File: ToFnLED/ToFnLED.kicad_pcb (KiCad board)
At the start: 2 copper layers, 37 x 10 mm, 10 parts, among them J1 Conn_01x04, J2 Conn_01x04, U1 PCA9632DP2_118, U2 VL53L1CXV0FY1

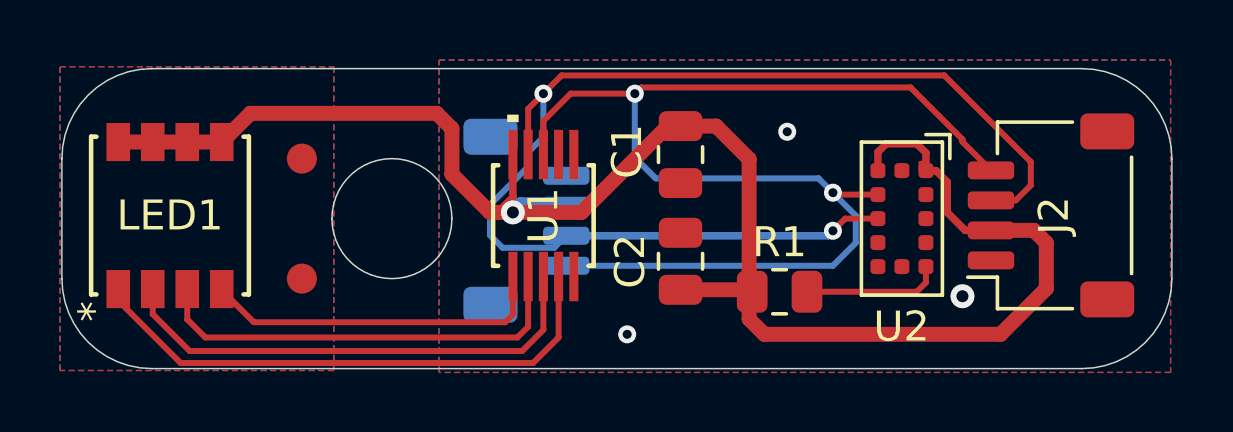
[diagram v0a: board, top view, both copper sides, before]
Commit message: Reversed LED connections
Reversed LED connections to match that of Someluckys version of the ToFnLED.
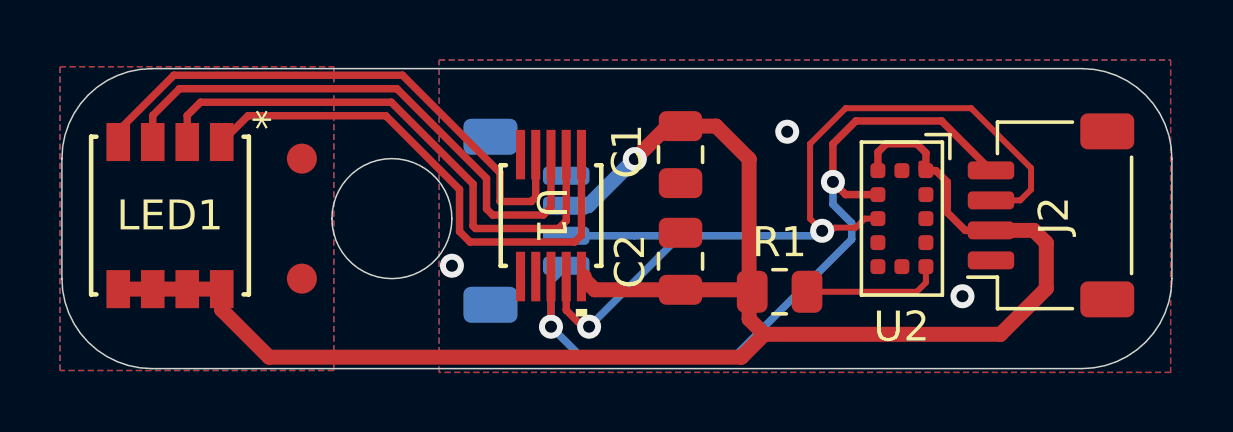
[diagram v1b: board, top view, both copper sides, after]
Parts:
- moved U1 0.25 mm to (145.5, 99.9), turned to -90 degrees
- turned LED1 to -90 degrees
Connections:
- U1 pad 1: Net-(LED1-ANODE_WHITE) -> Net-(LED1-ANODE_RED)
- U1 pad 2: Net-(LED1-ANODE_BLUE) -> Net-(LED1-ANODE_GREEN)
- U1 pad 3: Net-(LED1-ANODE_GREEN) -> Net-(LED1-ANODE_BLUE)
- U1 pad 4: Net-(LED1-ANODE_RED) -> Net-(LED1-ANODE_WHITE)
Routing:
- net /SCL: track 40.4 -> 27.4 mm
- net /SDA: track 41.2 -> 31.0 mm
- net Net-(LED1-ANODE_WHITE): track 11.6 -> 18.8 mm
- net +3.3V: track 58.1 -> 63.1 mm
- net Net-(LED1-ANODE_BLUE): track 14.4 -> 18.7 mm
- net Net-(LED1-ANODE_GREEN): track 16.4 -> 18.6 mm
- net Net-(LED1-ANODE_RED): track 18.3 -> 17.7 mm
